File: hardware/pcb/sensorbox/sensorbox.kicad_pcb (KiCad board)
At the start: 2 copper layers, 65 x 85 mm, 8 parts, among them U1 NodeMCU_D1, U2 MH-Z14A, U3 BME280, U4 OLED-Display-0.69

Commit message: Final pcb design
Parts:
- added D1: LED, LED_THT:LED_D3.0mm, F.Cu at (26.0, 80.0)
- added D2: LED, LED_THT:LED_D3.0mm, F.Cu at (32.0, 80.0)
- added D3: LED, LED_THT:LED_D3.0mm, F.Cu at (38.0, 80.0)
- added Q1: 2N7002, Package_TO_SOT_SMD:SOT-23, B.Cu at (32.0, 69.0)
- added Q2: 2N7002, Package_TO_SOT_SMD:SOT-23, B.Cu at (38.0, 69.0)
- added Q3: 2N7002, Package_TO_SOT_SMD:SOT-23, B.Cu at (44.0, 69.0)
- added R1: 4.7k, Resistor_SMD:R_0805_2012Metric, B.Cu at (18.0, 76.0)
- added R2: 4.7k, Resistor_SMD:R_0805_2012Metric, B.Cu at (18.0, 78.0)
- added R3: 330, Resistor_SMD:R_0805_2012Metric, B.Cu at (29.0, 75.0)
- added R4: 330, Resistor_SMD:R_0805_2012Metric, B.Cu at (35.0, 75.0)
- added R5: 330, Resistor_SMD:R_0805_2012Metric, B.Cu at (41.0, 75.0)
- added SW1: Dark Mode, Button_Switch_THT:SW_PUSH_6mm, F.Cu at (47.0, 77.0)
- added U5: OLED-Display-0.69, sensorbox:OLED-Display-0.69, F.Cu at (49.0, 60.0)
- moved U3 10.0 mm to (17.0, 79.0)
- moved U2 2.00 mm to (61.0, 44.0)
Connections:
- U1 pad 1: Net-(U1-Pad1) -> 5V
- U1 pad 11: Net-(U1-Pad11) -> RED
- U1 pad 12: Net-(U1-Pad12) -> YELLOW
- U1 pad 13: Net-(U1-Pad13) -> GREEN
- U1 pad 2: Net-(U1-Pad2) -> GND
- U1 pad 4: Net-(U1-Pad4) -> DARK
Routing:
- net GND: track 0.00 -> 172.3 mm, vias 0 -> 2
- net 5V: track 0.00 -> 123.4 mm
- net 3V3: track 0.00 -> 115.6 mm
- net SDA: track 0.00 -> 80.3 mm, vias 0 -> 2
- net SCL: track 0.00 -> 79.8 mm
- net S2: track 0.00 -> 51.5 mm
- net S1: track 0.00 -> 48.7 mm
- net DARK: track 0.00 -> 45.7 mm
- net RED: track 0.00 -> 44.3 mm, vias 0 -> 1
- net YELLOW: track 0.00 -> 39.1 mm, vias 0 -> 1
- net GREEN: track 0.00 -> 35.5 mm, vias 0 -> 1
- net Net-(D3-Pad1): track 0.00 -> 17.7 mm, vias 0 -> 1
- net Net-(D2-Pad1): track 0.00 -> 17.6 mm, vias 0 -> 1
- net Net-(D1-Pad1): track 0.00 -> 17.6 mm, vias 0 -> 1
- net Net-(D3-Pad2): track 0.00 -> 4.25 mm
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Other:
- outline, holes or cut-outs redrawn
- rule trace_min: 0.2 -> 0.127

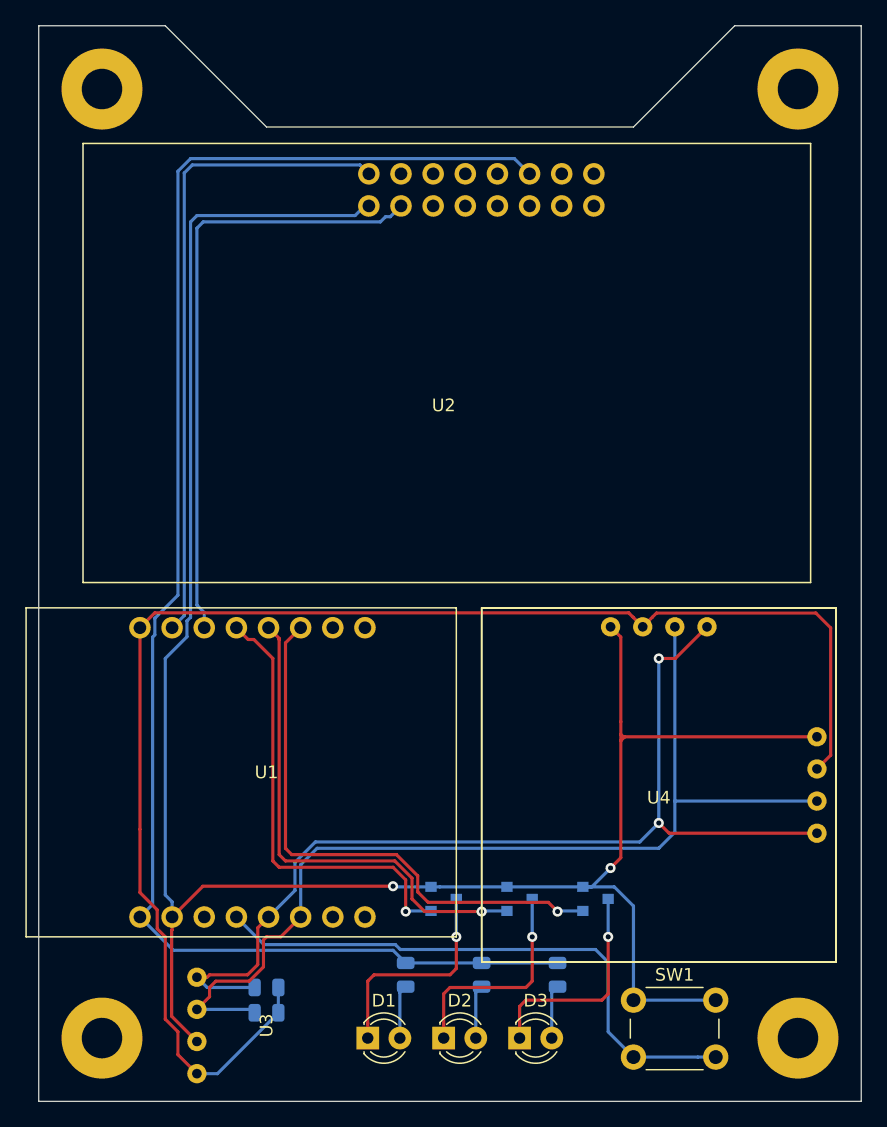
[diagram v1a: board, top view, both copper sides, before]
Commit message: Increased all hole sizes to 1mm
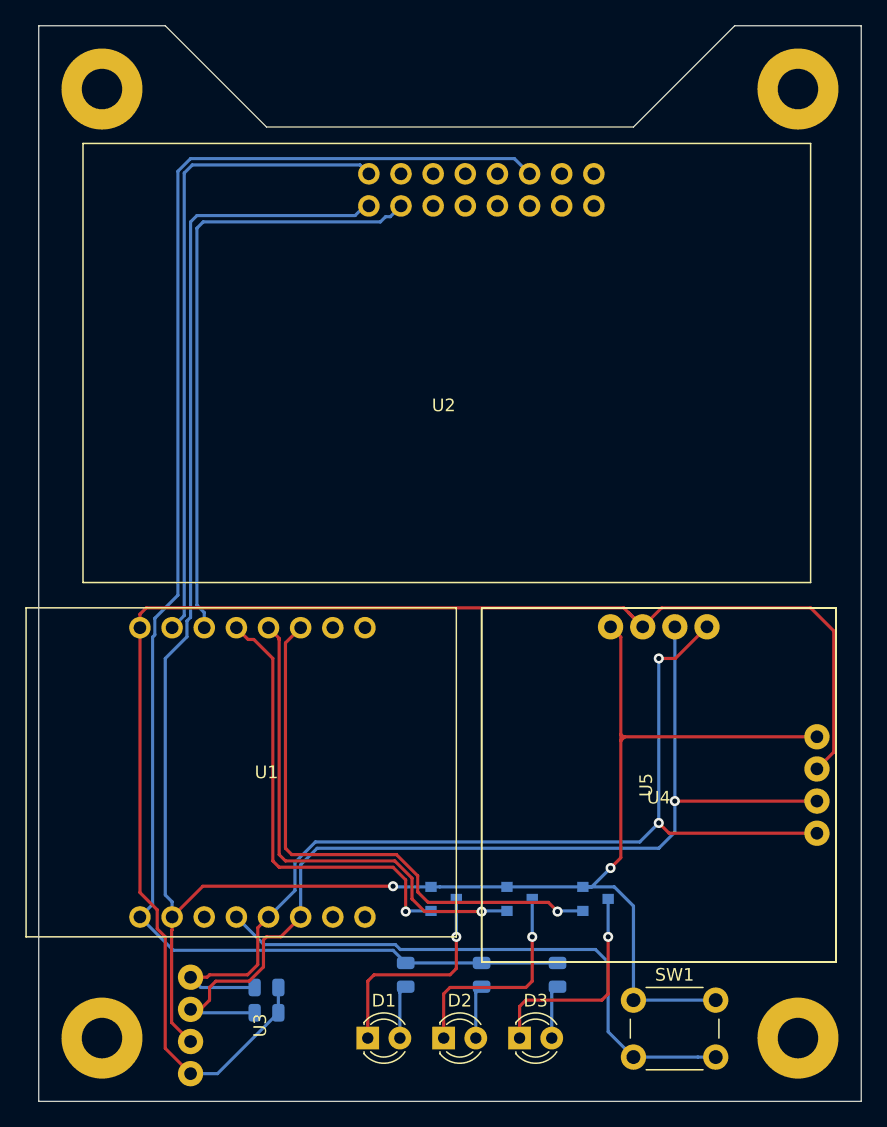
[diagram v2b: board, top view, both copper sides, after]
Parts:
- moved U3 0.50 mm to (16.5, 79.0)
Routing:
- net 3V3: track 115.6 -> 118.4 mm
- net SCL: track 79.8 -> 81.3 mm, vias 0 -> 1
- net SDA: track 80.3 -> 81.3 mm

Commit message: Board redesign
- Move BME280 far away from MCU
- Move display, LEDs and button next to each other
- Rotate MCU to route cable out towards the bottom
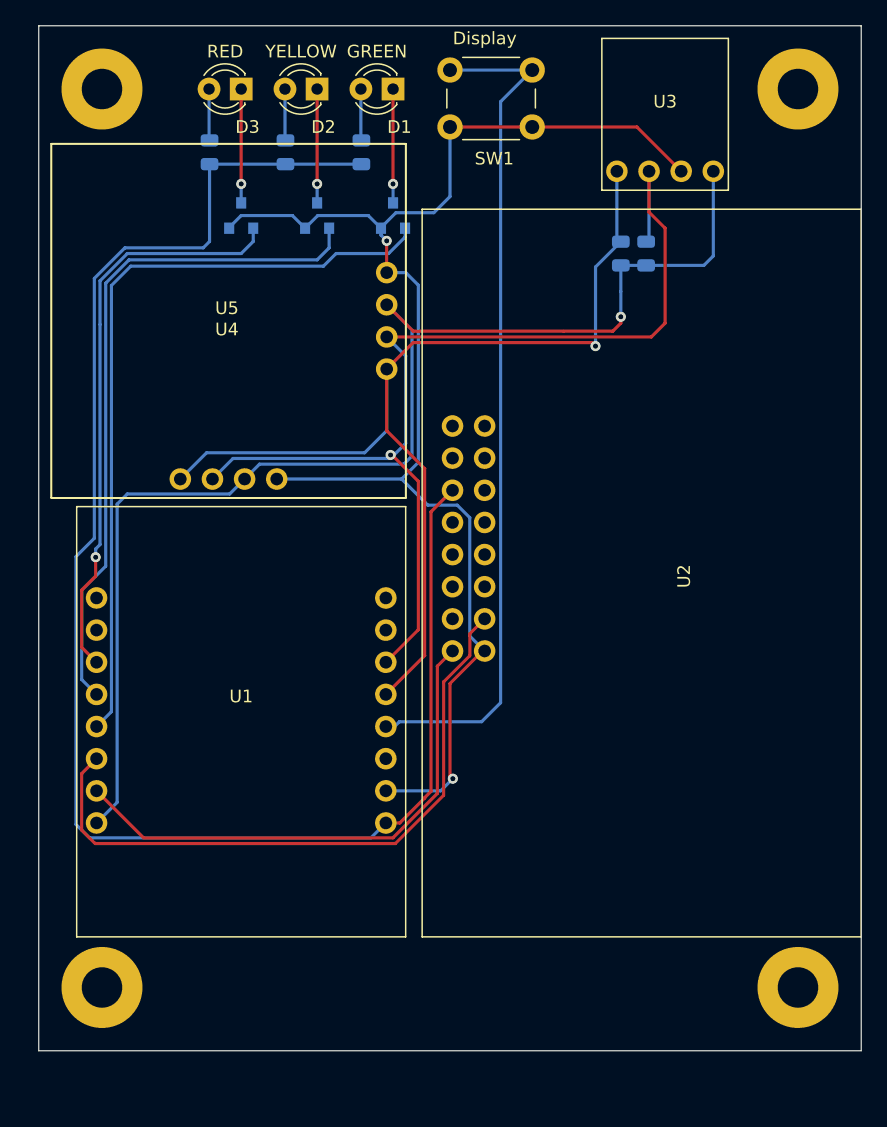
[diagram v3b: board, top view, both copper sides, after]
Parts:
- removed the REF** at (60.0, 80.0)
- removed the REF** at (5.00, 80.0)
- added REF**: MountingHole_3.2mm_M3_Pad, MountingHole:MountingHole_3.2mm_M3_Pad, F.Cu at (60.0, 76.0)
- added REF**: MountingHole_3.2mm_M3_Pad, MountingHole:MountingHole_3.2mm_M3_Pad, F.Cu at (5.00, 76.0)
- D1: value LED -> GREEN
- D2: value LED -> YELLOW
- D3: value LED -> RED
- SW1: value Dark Mode -> Display
- moved U3 79.2 mm to (49.5, 7.00), turned to 180 degrees
- moved D3 78.2 mm to (16.0, 5.00), turned to 180 degrees
- moved D2 75.7 mm to (22.0, 5.00), turned to 180 degrees
- moved D1 75.0 mm to (28.0, 5.00), turned to 180 degrees
- moved R5 70.6 mm to (13.5, 10.0), turned to 90 degrees
- moved SW1 69.5 mm to (39.0, 8.00), turned to 180 degrees
- moved R2 67.1 mm to (48.0, 18.0), turned to 90 degrees
- moved R4 66.8 mm to (19.5, 10.0), turned to 90 degrees
- moved R3 65.1 mm to (25.5, 10.0), turned to 90 degrees
- moved R1 64.4 mm to (46.0, 18.0), turned to 90 degrees
- moved Q3 60.8 mm to (16.0, 15.0), turned to 90 degrees
- moved Q2 56.3 mm to (22.0, 15.0), turned to 90 degrees
- moved Q1 54.1 mm to (28.0, 15.0), turned to 90 degrees
- moved U4 50.0 mm to (15.0, 23.3), turned to 270 degrees
- moved U5 50.0 mm to (15.0, 23.3), turned to 180 degrees
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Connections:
- net DARK renamed DISPLAY
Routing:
- net GND: track 172.2 -> 113.1 mm
- net GREEN: track 35.5 -> 60.8 mm, vias 1 -> 0
- net DISPLAY: track 45.7 -> 67.4 mm
- net 3V3: track 118.4 -> 102.0 mm, vias 0 -> 1
- net YELLOW: track 39.1 -> 54.1 mm, vias 1 -> 0
- net S2: track 51.5 -> 41.7 mm
- net Net-(D3-Pad1): track 17.7 -> 9.00 mm
- net Net-(D2-Pad1): track 17.6 -> 9.00 mm
- net Net-(D1-Pad1): track 17.6 -> 9.00 mm
- net S1: track 48.7 -> 52.0 mm
- net 5V: track 123.4 -> 126.7 mm
- net SCL: track 81.3 -> 84.5 mm
- net SDA: track 81.3 -> 83.2 mm, vias 2 -> 1
- net RED: track 44.3 -> 45.7 mm
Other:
- board size 65 x 85 mm -> 65 x 81 mm

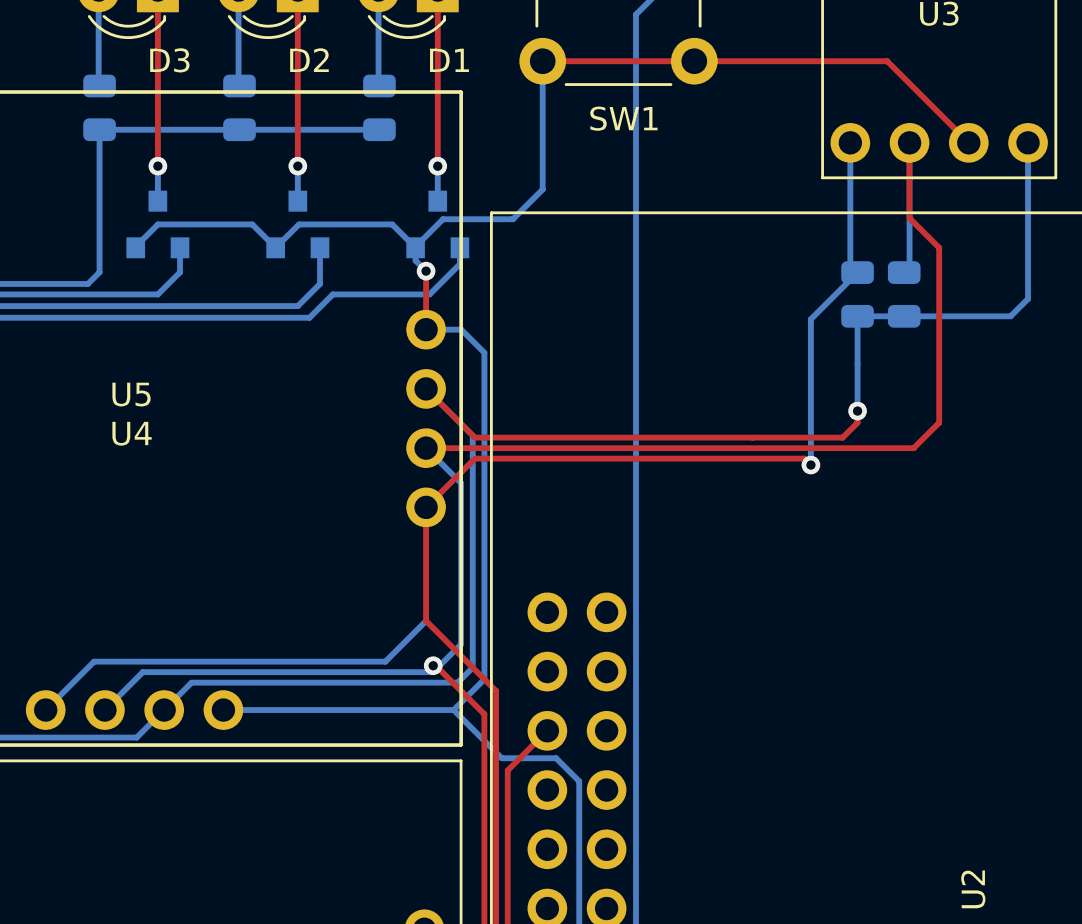
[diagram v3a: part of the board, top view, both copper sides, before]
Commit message: Optimize traces.
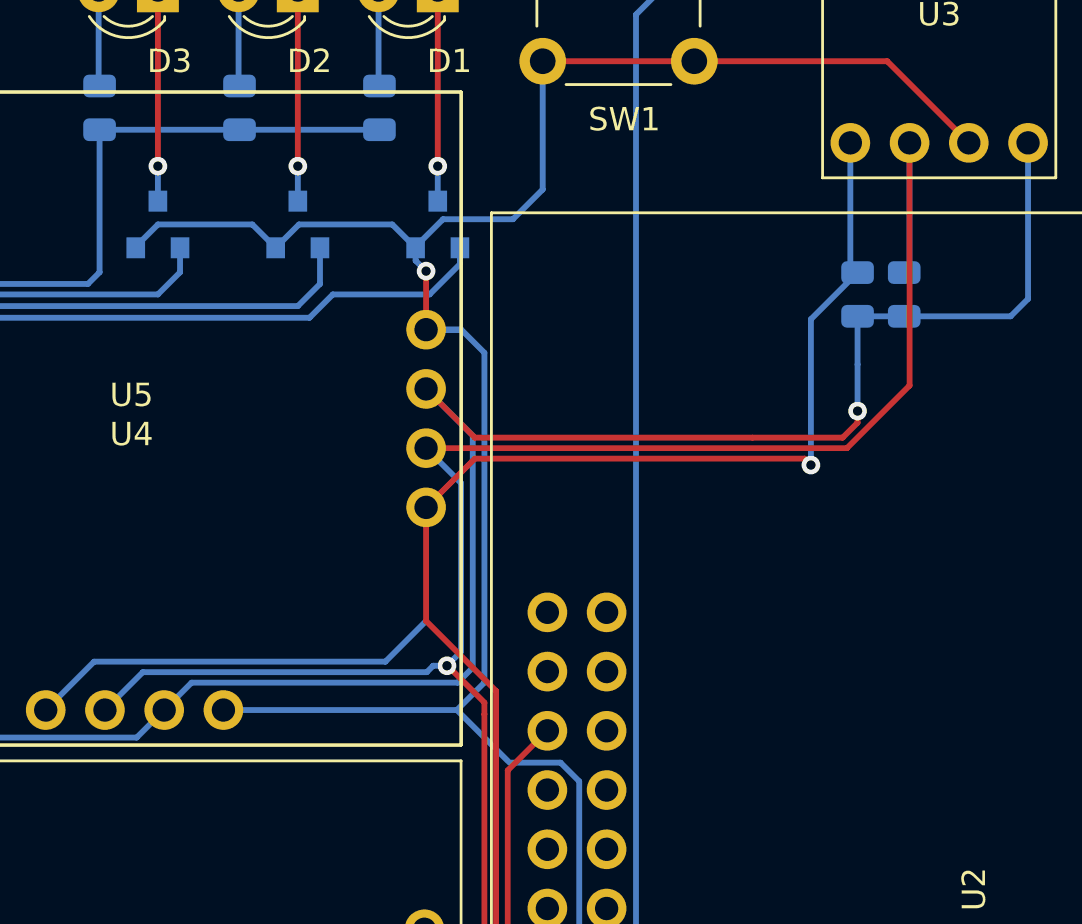
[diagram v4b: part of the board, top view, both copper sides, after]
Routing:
- net SCL: track 84.5 -> 81.7 mm
- net GND: track 113.1 -> 114.4 mm

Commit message: Add name and author.
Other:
- board text added: "Sensorbox 0.2"
- board text added: "by Michael Würtinger"

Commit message: Add order number placement label
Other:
- board text added: "JLCJLCJLCJLC"
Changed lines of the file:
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@@
   (general
     (thickness 1.6)
-    (drawings 6)
+    (drawings 7)
     (tracks 178)
     (zones 0)
@@
     (pad 1 thru_hole circle (at 0 0) (size 6.4 6.4) (drill 3.2) (layers *.Cu *.Mask))
   )
+  (gr_text JLCJLCJLCJLC (at 32.5 78) (layer B.SilkS)
+    (effects (font (size 1 1) (thickness 0.15)))
+  )
   (gr_text "by Michael Würtinger" (at 27.25 78) (layer F.SilkS)
